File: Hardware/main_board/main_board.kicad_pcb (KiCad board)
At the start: 6 copper layers, 95.4 x 36.1 mm, 280 parts, among them J1 BATT, J2 LCD, J3 BACK_LIGHT, J4 SD, J5 NFC, J6 EXT1, J7 EXT0, J8 USB_C, Q1 DMN313DLT, SW1 OK, SW2 BACK, SW3 RIGHT, SW4 LEFT, SW5 UP, SW6 DOWN, T1 B0310J50100AHF, U1 STM32WB55RGVx, U10 BGS13S4N9E6327XTSA1, U11 NC7SZ32M5X, U12 LP5562TMX, U2 BQ27220YZFR, U3 BQ25896RTWR, U4 RS3221-3.3YF3, U5 LM66100DCK, U6 LM3281YFQR, U7 LM3281YFQR, U8 CC1101RGP, U9 BGS13S4N9E6327XTSA1, Y1 32MHz, Y2 32.768K, Y3 26MHz

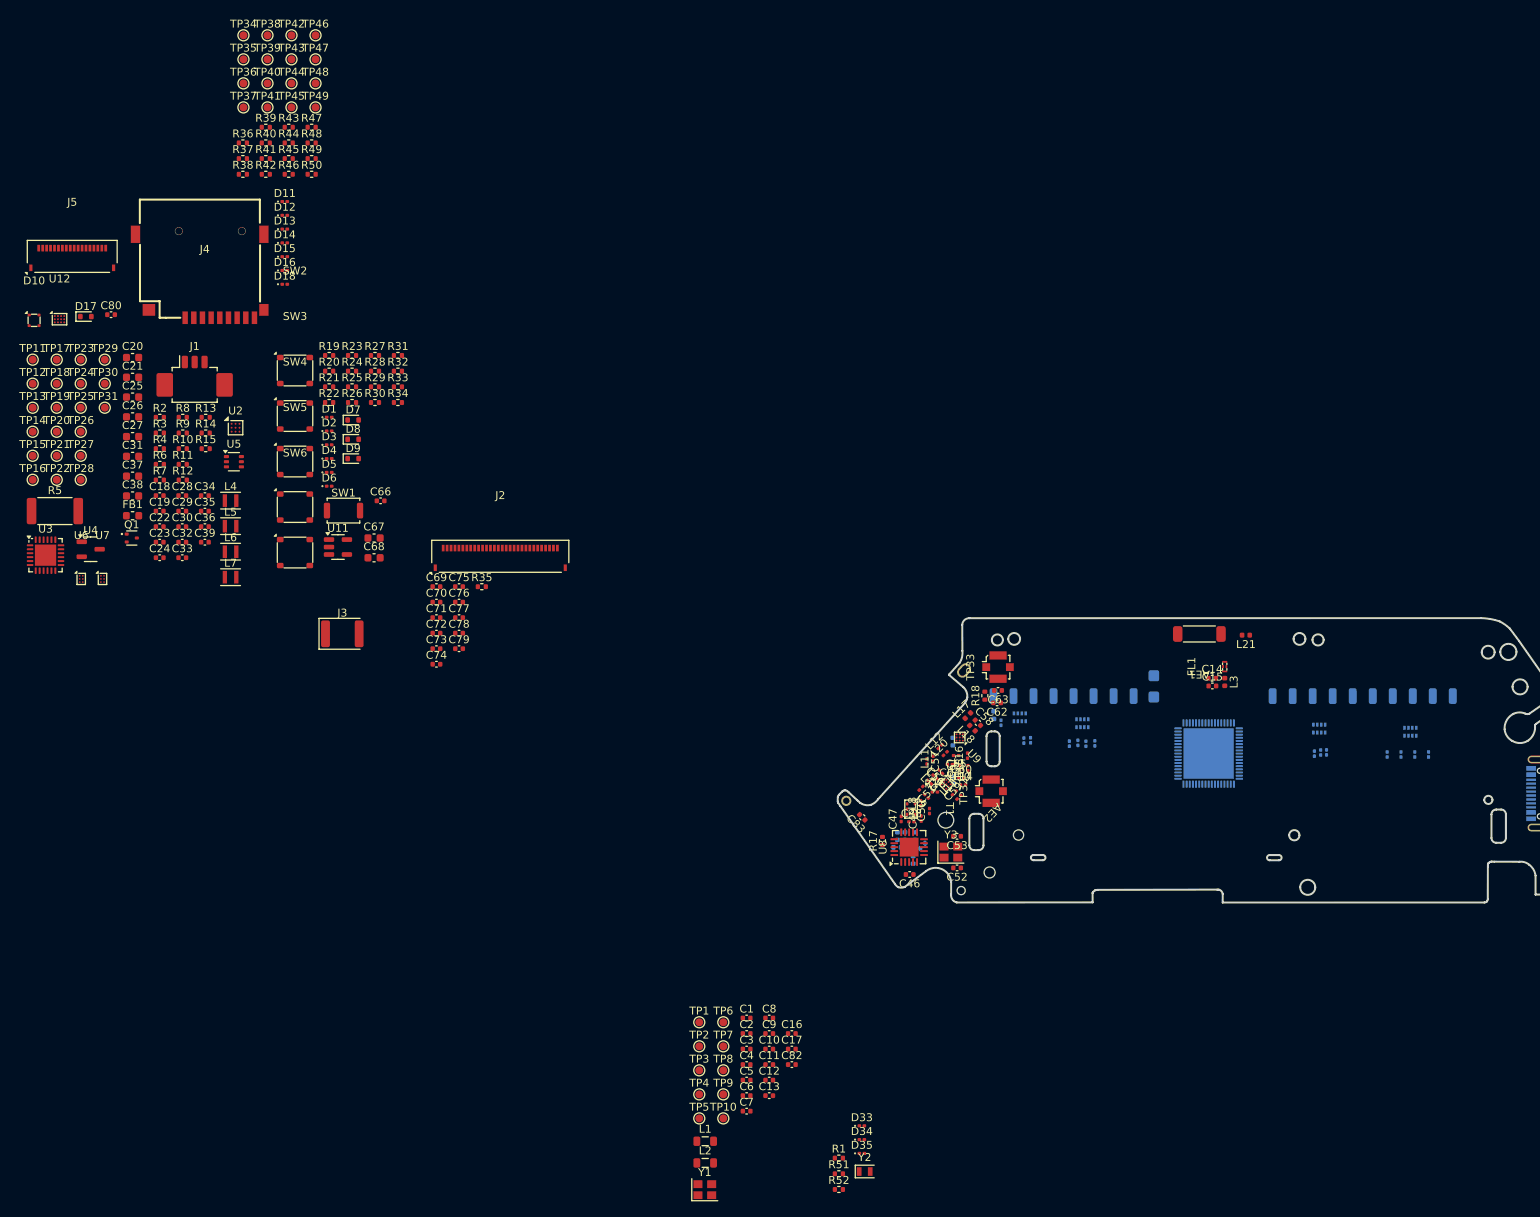
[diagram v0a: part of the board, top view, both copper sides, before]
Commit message: layout: finish the Sub-1G filter
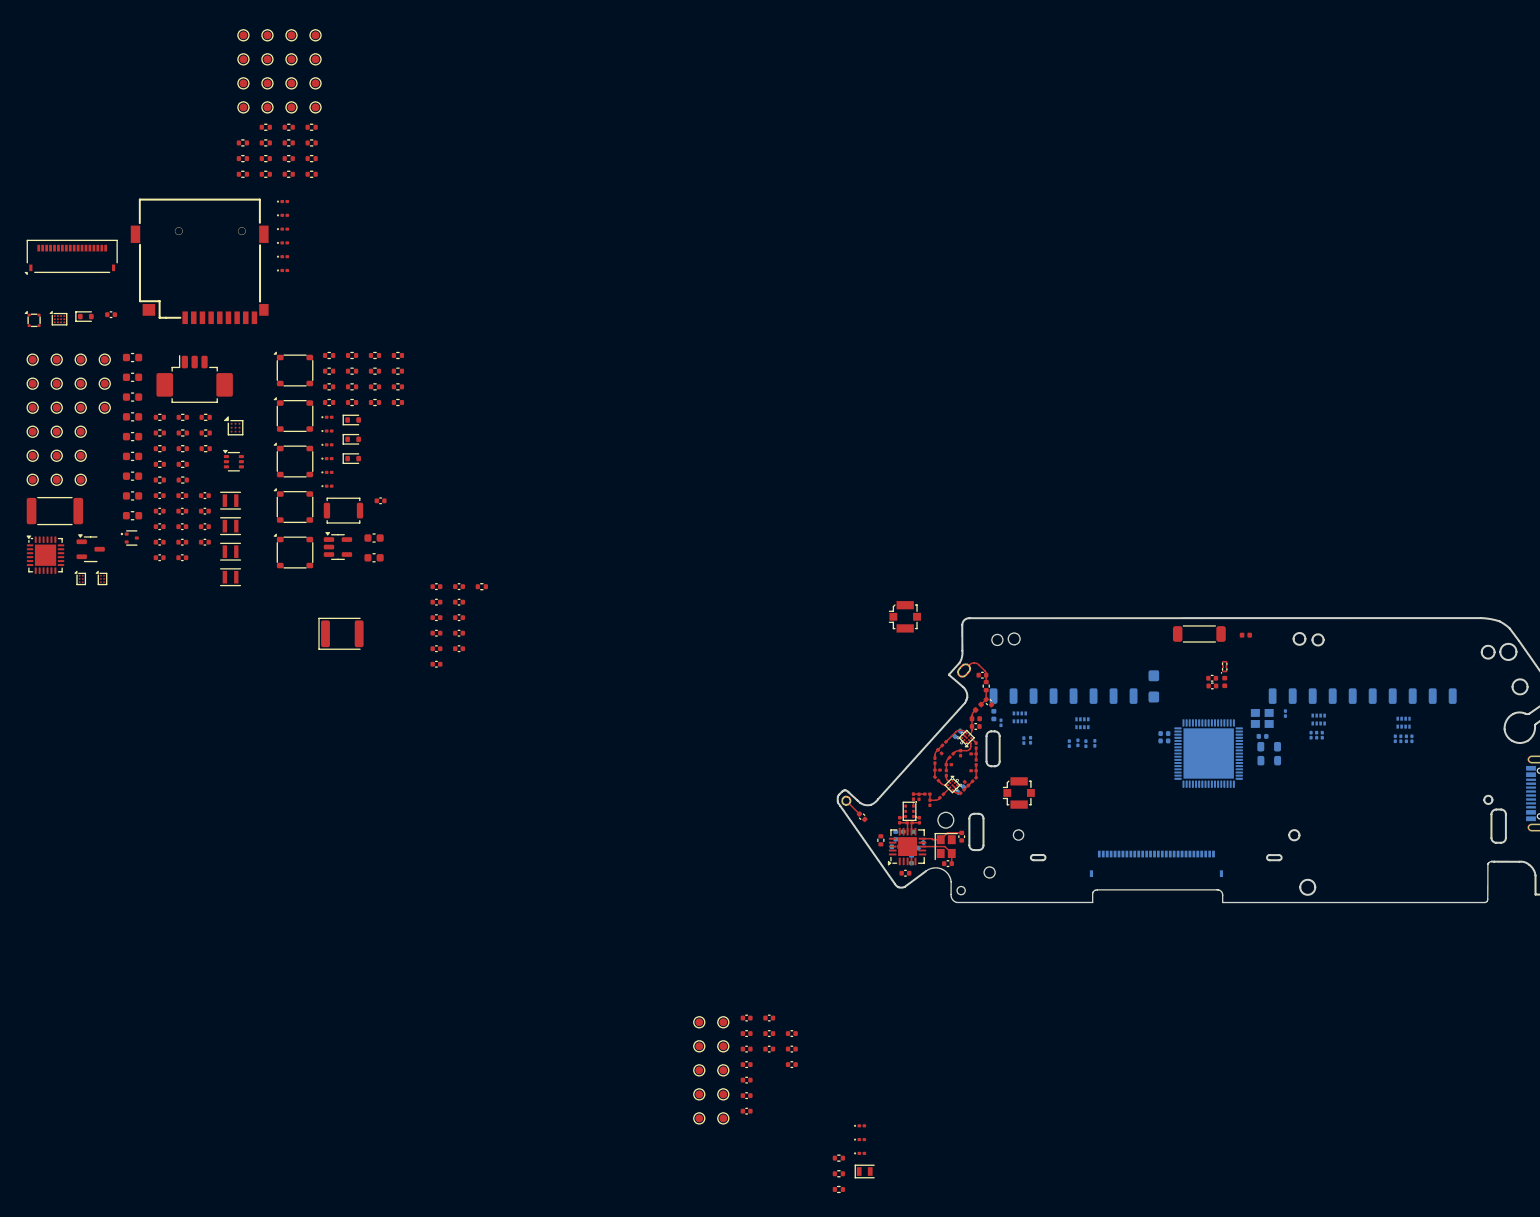
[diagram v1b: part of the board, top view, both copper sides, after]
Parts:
- C11, C12, C13, D18, J2, L1, L2, Y1: moved to B.Cu
- moved D18 138.2 mm to (217.9, 124.2), turned to 90 degrees
- moved Y1 92.7 mm to (215.0, 124.8)
- moved J2 91.9 mm to (201.5, 143.0), turned to 180 degrees
- moved L2 87.9 mm to (215.8, 130.2), turned to 180 degrees
- moved L1 87.4 mm to (215.8, 128.4)
- moved C11 75.2 mm to (215.0, 127.1), turned to 180 degrees
- moved C13 68.0 mm to (202.5, 126.7)
- moved C12 66.1 mm to (202.5, 127.6)
- moved TP33 13.4 mm to (169.6, 111.9)
- moved TP32 3.56 mm to (184.1, 134.2)
- moved D29 2.90 mm to (234.0, 127.4)
- moved C63 2.78 mm to (179.4, 119.3), turned to 0 degrees
- moved C61 2.52 mm to (178.3, 129.3), turned to 0 degrees
- moved D28 2.38 mm to (221.2, 126.9)
- moved D30 2.26 mm to (233.3, 127.4)
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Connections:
- T1 pad 5: Net-(T1-DNC) -> unconnected-(T1-NC-Pad5)
- T1 pad 6: Net-(T1-DNC) -> unconnected-(T1-NC-Pad6)
- Y1 pad 3: GND -> Net-(U1-OSC_IN)
- Y1 pad 4: Net-(U1-OSC_IN) -> GND
- Y3 pad 1: Net-(U8-XOSC_Q1) -> Net-(U8-XOSC_Q2)
- Y3 pad 3: GND -> Net-(U8-XOSC_Q1)
- Y3 pad 4: Net-(U8-XOSC_Q2) -> GND
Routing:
- net /CC1101/RF_SW_1: track 0.00 -> 5.79 mm, vias 0 -> 2
- net /CC1101/RF_SW_0: track 0.00 -> 5.79 mm, vias 0 -> 2
- net Net-(U8-XOSC_Q2): track 0.00 -> 5.39 mm
- net Net-(U8-XOSC_Q1): track 0.00 -> 5.37 mm
- net Net-(AE2-A): track 0.00 -> 4.86 mm
- net Net-(U10-RF3): track 0.00 -> 3.54 mm
- net Net-(U10-RFIN): track 0.00 -> 3.54 mm
- net Net-(U10-RF2): track 0.00 -> 3.34 mm
- net Net-(AE2-Shield): track 0.00 -> 2.37 mm
- net Net-(C51-Pad2): track 0.00 -> 2.15 mm
- net Net-(U8-RF_P): track 0.00 -> 2.10 mm
- net Net-(U8-RF_N): track 0.00 -> 2.10 mm
- net Net-(C62-Pad2): track 0.00 -> 2.10 mm
- net Net-(C57-Pad1): track 0.00 -> 1.97 mm
- net Net-(C64-Pad2): track 0.00 -> 1.81 mm
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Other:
- outline, holes or cut-outs redrawn

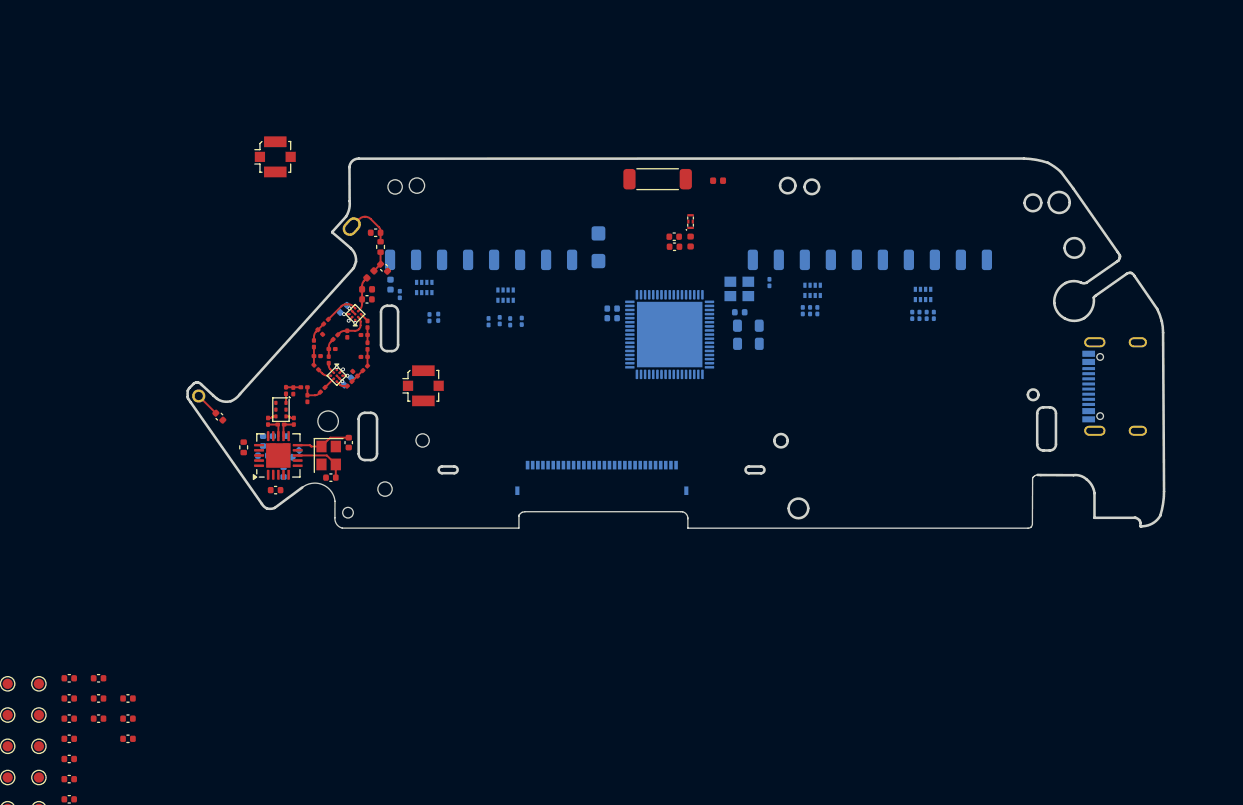
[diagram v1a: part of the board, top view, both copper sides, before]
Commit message: layout: optimise cc1101 and start the stm32
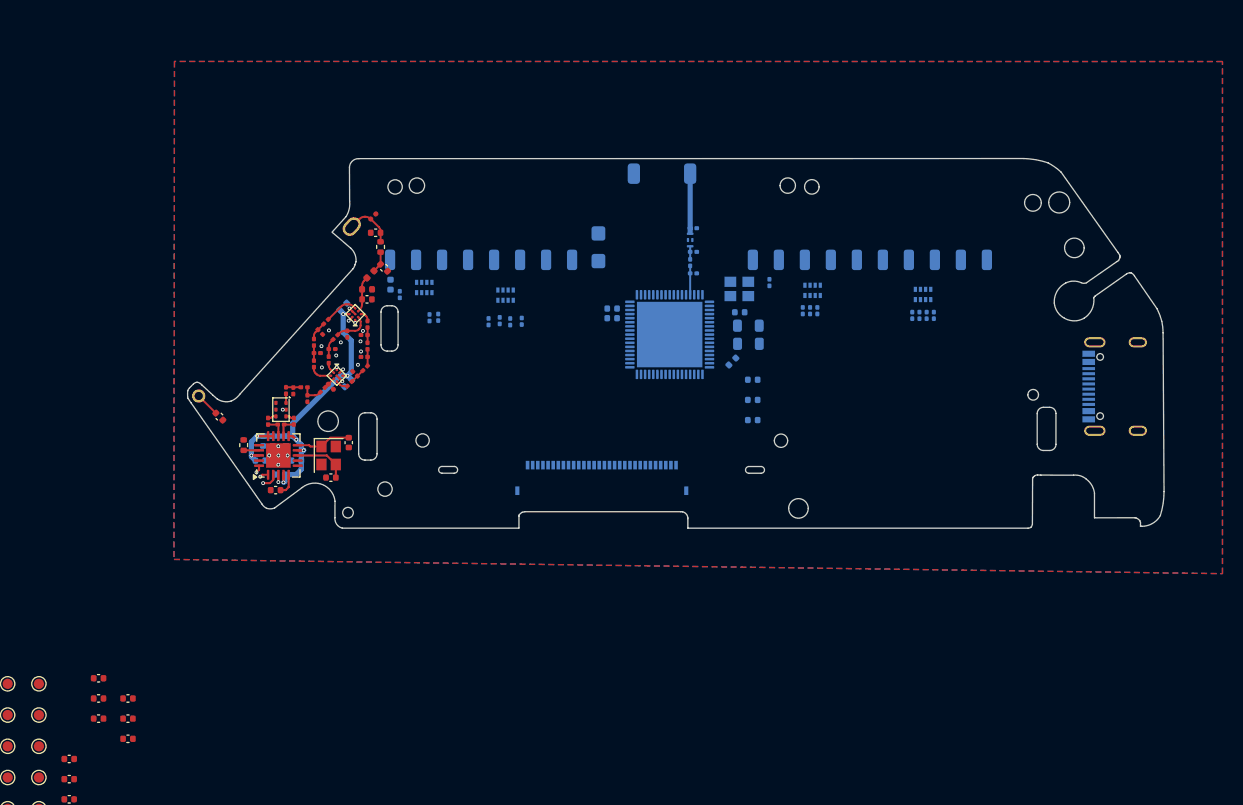
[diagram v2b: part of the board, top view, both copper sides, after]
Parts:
- AE1, C1, C2, C3, C4, FL1: moved to B.Cu
- C14, C15: footprint Capacitor_SMD:C_0402_1005Metric -> Capacitor_SMD:C_0201_0603Metric; moved to B.Cu
- L21, L3: footprint Inductor_SMD:L_0402_1005Metric -> Inductor_SMD:L_0201_0603Metric; moved to B.Cu
- TP32, TP33: footprint Connector_Coaxial:U.FL_Molex_MCRF_73412-0110_Vertical -> Library:TP_DP
- moved C2 73.7 mm to (216.3, 133.7), turned to 180 degrees
- moved C3 73.7 mm to (216.3, 135.6), turned to 180 degrees
- moved C4 73.7 mm to (216.3, 137.6), turned to 180 degrees
- moved C1 71.8 mm to (214.3, 131.9), turned to 45 degrees
- moved TP33 11.2 mm to (179.2, 117.7), turned to 45 degrees
- moved TP32 9.04 mm to (175.1, 134.3), turned to -45 degrees
- moved L21 5.23 mm to (210.5, 118.9)
- moved C15 3.19 mm to (210.5, 123.3), turned to 180 degrees
- moved C14 2.39 mm to (210.5, 121.2), turned to 180 degrees
- moved L3 2.06 mm to (210.2, 122.2)
- moved FL1 1.80 mm to (210.2, 120.0)
- moved AE1 0.69 mm to (207.4, 113.5)
- moved C41 0.66 mm to (171.7, 141.6), turned to 0 degrees
- moved C45 0.54 mm to (168.2, 141.6)
- moved C44 0.44 mm to (170.1, 142.9), turned to 0 degrees
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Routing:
- net +3.3V: track 1.01 -> 34.6 mm, vias 2 -> 7
- net /CC1101/RF_SW_1: track 5.79 -> 20.1 mm, vias 2 -> 3
- net Net-(AE1-FEED): track 0.00 -> 5.74 mm
- net Net-(U1-RF1): track 0.00 -> 2.80 mm
- net Net-(U8-DCOUPL): track 0.00 -> 2.12 mm
- net /CC1101/SPI_R_MISO: track 0.00 -> 1.61 mm, vias 0 -> 1
- net Net-(U8-RBIAS): track 0.00 -> 1.50 mm
- net Net-(FL1-IN): track 0.00 -> 1.27 mm
- net /CC1101/SPI_R_SCK: track 0.00 -> 0.85 mm, vias 0 -> 1
- net Net-(U9-RF1): track 1.41 -> 2.22 mm
- net /CC1101/SPI_R_MOSI: track 0.00 -> 0.75 mm, vias 0 -> 1
- net GND: vias 2 -> 17
- added copper zone on B.Cu, net GND
- added copper zone on F.Cu, net GND
- added copper zone on In1.Cu, net GND
- added copper zone on In4.Cu, net GND
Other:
- outline, holes or cut-outs redrawn

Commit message: layout: layout some of SMPSs
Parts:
- added NT1: NetTie, NetTie:NetTie-2_SMD_Pad0.5mm, F.Cu at (236.6, 146.6)
- C10, C16, C17, C31, C37, C38, C5, C6, C7, C8, C9, J4, L5, L6, L7, R1, U3, U6, U7: moved to B.Cu
- C29, C34, C35, C39: footprint Capacitor_SMD:C_0402_1005Metric -> Capacitor_SMD:C_0201_0603Metric; moved to B.Cu
- C30: footprint Capacitor_SMD:C_0402_1005Metric -> Capacitor_SMD:C_0603_1608Metric
- C36: footprint Capacitor_SMD:C_0402_1005Metric -> Capacitor_SMD:C_0603_1608Metric; moved to B.Cu
- L1: footprint Inductor_SMD:L_0805_2012Metric -> Inductor_SMD:L_0603_1608Metric
- R15: footprint Resistor_SMD:R_0402_1005Metric -> Resistor_SMD:R_0201_0603Metric; moved to B.Cu
- Y2: footprint Crystal:Crystal_SMD_2012-2Pin_2.0x1.2mm -> Crystal:Crystal_SMD_3215-2Pin_3.2x1.5mm; moved to B.Cu
- moved C18 214.6 mm to (283.9, 145.5)
- moved C19 214.6 mm to (283.9, 147.4)
- moved C20 214.6 mm to (280.5, 127.9)
- moved C21 214.6 mm to (280.5, 130.4)
- moved C22 214.6 mm to (283.9, 149.4)
- moved C23 214.6 mm to (283.9, 151.4)
- moved C24 214.6 mm to (283.9, 153.3)
- moved C25 214.6 mm to (280.5, 133.0)
- moved C26 214.6 mm to (280.5, 135.5)
- moved C27 214.6 mm to (280.5, 138.0)
- moved FB1 214.6 mm to (280.5, 148.0)
- moved Q1 214.6 mm to (280.4, 150.8)
- moved R13 214.6 mm to (289.8, 135.5)
- moved R14 214.6 mm to (289.8, 137.5)
- moved R2 214.6 mm to (283.9, 135.5)
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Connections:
- C18 pad 2: /Power/BAT_TEST -> /Power/BAT+
- C30 pad 1: GND -> PGND
- C31 pad 1: GND -> PGND
- C36 pad 1: GND -> PGND
- C37 pad 1: GND -> PGND
- C38 pad 1: GND -> unconnected-(C38-Pad1)
- J1 pad 1: /Power/BAT_TEST -> GND
- J1 pad 3: GND -> /Power/BAT+
- R5 pad 1: BAT -> /Power/BAT-
- R5 pad 2: /Power/BAT_TEST -> /Power/BAT+
- TP14 pad 1: /Power/BAT_TEST -> /Power/BAT+
- TP15 pad 1: /Power/BAT_TEST -> /Power/BAT+
- U2 pad C1: /Power/BAT_TEST -> /Power/BAT+
- U2 pad C2: BAT -> /Power/BAT-
- U2 pad C3: /Power/BAT_TEST -> /Power/BAT+
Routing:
- net /Power/BAT-: track 0.00 -> 10.9 mm
- net /Power/BAT+: track 0.00 -> 10.9 mm
- net VSYS: track 0.00 -> 2.71 mm
- net Net-(U7-SW): track 0.00 -> 2.39 mm, vias 0 -> 2
- net Net-(U6-SW): track 0.00 -> 2.39 mm, vias 0 -> 2
- net GND: track 1.56 -> 2.88 mm, vias 17 -> 18
- net +3.3V_EXT: track 0.00 -> 0.98 mm
- net Net-(U7-FB): track 0.00 -> 0.98 mm
- net /MCU/PERI_EN: track 0.00 -> 0.93 mm
- added copper zone on F.Cu, net /Power/BAT+

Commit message: layout: layout SMPSs and the bms
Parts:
- added FB2: 120R@100MHz, Inductor_SMD:L_0603_1608Metric, B.Cu at (233.5, 129.5)
- C19, C20, C21, C24, C25, C30, FB1, L4, Q1, R4, R6, R7, U4: moved to B.Cu
- moved U4 74.7 mm to (202.4, 135.2), turned to 180 degrees
- moved C30 67.9 mm to (226.7, 130.6), turned to -90 degrees
- moved C26 61.2 mm to (237.1, 92.3)
- moved C27 61.2 mm to (237.1, 94.8)
- moved R12 61.2 mm to (243.5, 100.3)
- moved R10 61.2 mm to (243.5, 96.4)
- moved R13 61.2 mm to (246.4, 92.4)
- moved R8 61.2 mm to (243.5, 92.4)
- moved R14 61.2 mm to (246.4, 94.4)
- moved R9 61.2 mm to (243.5, 94.4)
- moved C28 61.2 mm to (243.4, 102.3)
- moved FB1 57.4 mm to (227.0, 127.1), turned to 90 degrees
- moved L4 55.1 mm to (241.4, 126.3), turned to -90 degrees
- moved C19 45.6 mm to (244.5, 124.5), turned to 180 degrees
- moved C24 44.9 mm to (248.4, 125.9), turned to -90 degrees
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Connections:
- C29 pad 1: GND -> GNDP
- C30 pad 1: PGND -> GNDP
- C31 pad 1: PGND -> GNDP
- C34 pad 1: PGND -> GNDP
- C35 pad 1: GND -> GNDP
- C36 pad 1: PGND -> GNDP
- C37 pad 1: PGND -> GNDP
- C38 pad 1: unconnected-(C38-Pad1) -> GNDP
- C39 pad 1: PGND -> GNDP
- FB1 pad 1: PGND -> GNDP
- TP30 pad 1: PGND -> GND
- TP31 pad 1: PGND -> GND
- U3 pad 17: PGND -> GND
- U3 pad 18: PGND -> GND
- U3 pad 25: PGND -> GND
- U6 pad C2: PGND -> GNDP
- U7 pad C2: PGND -> GNDP
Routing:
- net /Power/BAT+: track 10.9 -> 19.8 mm, vias 0 -> 2
- net VUSB: track 0.00 -> 3.60 mm
- net Net-(U3-PMID): track 0.00 -> 3.11 mm
- net Net-(Q1-D): track 0.00 -> 2.86 mm
- net Net-(U2-VDD): track 0.00 -> 2.84 mm
- net Net-(U3-PG_N): track 0.00 -> 2.82 mm
- net Net-(U3-STAT): track 0.00 -> 2.78 mm
- net /MCU/I2C_SCL: track 0.00 -> 2.30 mm, vias 0 -> 1
- net /MCU/I2C_SDA: track 0.00 -> 2.25 mm, vias 0 -> 1
- net Net-(U2-BIN): track 0.00 -> 1.85 mm
- net Net-(U2-GPOUT): track 0.00 -> 1.85 mm
- net Net-(U3-INT): track 0.00 -> 1.68 mm
- net Net-(U3-ILIM): track 0.00 -> 1.54 mm
- net Net-(U3-BTST): track 0.00 -> 1.14 mm
- net /Power/BAT-: track 10.9 -> 11.2 mm, vias 0 -> 1
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- added copper zone on B.Cu, net +3.3V
- added copper zone on B.Cu, net +3.3V_EXT
- added copper zone on B.Cu, net BAT
- added copper zone on B.Cu, net GNDP
- added copper zone on In1.Cu, net GNDP
- added copper zone on In2.Cu, net GNDP
- added copper zone on In3.Cu, net GNDP
- added copper zone on B.Cu, net Net-(U7-FB)
- added copper zone on B.Cu, net SW
- added copper zone on B.Cu, net VSYS
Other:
- outline, holes or cut-outs redrawn
